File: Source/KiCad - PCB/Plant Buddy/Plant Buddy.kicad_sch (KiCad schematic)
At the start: 25 parts, among them J1 Screw_Terminal_01x02, Q1 AO3401, U1 AMS1117-3.3, U2 TLC555xD

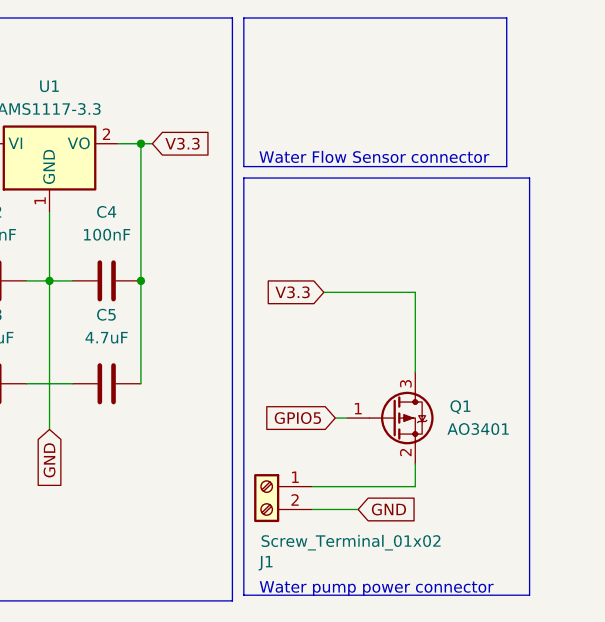
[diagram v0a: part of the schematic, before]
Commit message: Added water flow sensor connector
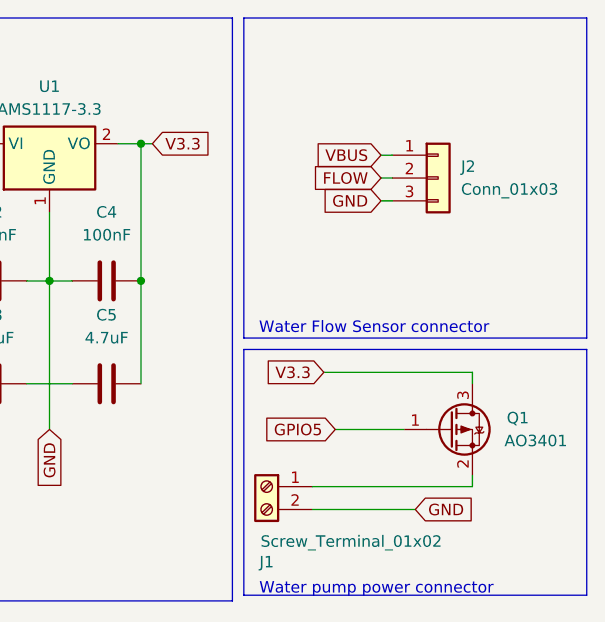
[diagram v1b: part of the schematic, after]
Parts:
- added J2: Conn_01x03, Connector_Hirose:Hirose_DF13-03P-1.25DSA_1x03_P1.25mm_Vertical, symbol Connector_Generic:Conn_01x03
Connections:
- net GND: now also J2.3 (Pin_3)
- net VBUS: now also J2.1 (Pin_1)
- new net FLOW: J2.2 (Pin_2)
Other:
- moved on the sheet: Q1
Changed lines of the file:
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@@
 	(rectangle
 		(start 212.09 13.97)
-		(end 241.3 30.48)
+		(end 250.19 49.53)
 		(stroke
 			(width 0)
@@
 	)
 	(rectangle
-		(start 212.09 31.75)
-		(end 243.84 78.105)
+		(start 212.09 50.8)
+		(end 250.19 78.105)
 		(stroke
 			(width 0)
@@
 	(text "Water Flow Sensor connector"
 		(exclude_from_sim no)
-		(at 226.568 29.718 0)
+		(at 226.568 48.514 0)
 		(effects
 			(font
@@
 	(wire
 		(pts
-			(xy 231.14 66.04) (xy 231.14 63.5)
+			(xy 237.49 66.04) (xy 237.49 64.77)
 		)
 		(stroke
@@
 	(wire
 		(pts
-			(xy 219.71 66.04) (xy 231.14 66.04)
+			(xy 219.71 66.04) (xy 237.49 66.04)
 		)
 		(stroke
@@
 	(wire
 		(pts
+			(xy 227.33 31.75) (xy 228.6 31.75)
+		)
+		(stroke
+			(width 0)
+			(type default)
+		)
+	)
+	(wire
+		(pts
 			(xy 190.5 35.56) (xy 190.5 59.69)
 		)
@@
 	(wire
 		(pts
-			(xy 219.71 68.58) (xy 224.79 68.58)
+			(xy 219.71 68.58) (xy 231.14 68.58)
 		)
 		(stroke
@@
 	(wire
 		(pts
+			(xy 227.33 29.21) (xy 228.6 29.21)
+		)
+		(stroke
+			(width 0)
+			(type default)
+		)
+	)
+	(wire
+		(pts
 			(xy 143.51 44.45) (xy 143.51 43.18)
 		)
@@
 	(wire
 		(pts
-			(xy 231.14 44.45) (xy 231.14 53.34)
+			(xy 237.49 53.34) (xy 237.49 54.61)
 		)
 		(stroke
@@
 	(wire
 		(pts
+			(xy 227.33 34.29) (xy 228.6 34.29)
+		)
+		(stroke
+			(width 0)
+			(type default)
+		)
+	)
+	(wire
+		(pts
 			(xy 118.11 62.23) (xy 127 62.23)
 		)
@@
 	(wire
 		(pts
-			(xy 220.98 44.45) (xy 231.14 44.45)
+			(xy 220.98 53.34) (xy 237.49 53.34)
 		)
 		(stroke
@@
 	(wire
 		(pts
-			(xy 222.25 58.42) (xy 223.52 58.42)
+			(xy 222.25 59.69) (xy 229.87 59.69)
 		)
 		(stroke
@@
 		)
 	)
+	(global_label "FLOW"
+		(shape input)
+		(at 227.33 31.75 180)
+		(fields_autoplaced yes)
+		(effects
+			(font
+				(size 1.27 1.27)
+			)
+			(justify right)
+		)
+		(property "Intersheetrefs" "${INTERSHEET_REFS}"
+			(at 219.4462 31.75 0)
+			(hide yes)
+			(show_name no)
+			(do_not_autoplace no)
+			(effects
+				(font
+					(size 1.27 1.27)
+				)
+				(justify right)
+			)
+		)
+	)
 	(global_label "VBAT"
 		(shape input)
@@
 		)
 	)
+	(global_label "VBUS"
+		(shape input)
+		(at 227.33 29.21 180)
+		(fields_autoplaced yes)
+		(effects
+			(font
+				(size 1.27 1.27)
+			)
+			(justify right)
+		)
+		(property "Intersheetrefs" "${INTERSHEET_REFS}"
+			(at 219.4462 29.21 0)
+			(hide yes)
+			(show_name no)
+			(do_not_autoplace no)
+			(effects
+				(font
+					(size 1.27 1.27)
+				)
+				(justify right)
+			)
+		)
+	)
 	(global_label "V3.3"
 		(shape input)
@@
 	(global_label "V3.3"
 		(shape input)
-		(at 220.98 44.45 180)
+		(at 220.98 53.34 180)
 		(fields_autoplaced yes)
 		(effects
@@
 		)
 		(property "Intersheetrefs" "${INTERSHEET_REFS}"
-			(at 213.8824 44.45 0)
+			(at 213.8824 53.34 0)
 			(hide yes)
 			(show_name no)
@@
 	(global_label "GND"
 		(shape input)
+		(at 227.33 34.29 180)
+		(fields_autoplaced yes)
+		(effects
+			(font
+				(size 1.27 1.27)
+			)
+			(justify right)
+		)
+		(property "Intersheetrefs" "${INTERSHEET_REFS}"
+			(at 220.4743 34.29 0)
+			(hide yes)
+			(show_name no)
+			(do_not_autoplace no)
+			(effects
+				(font
+					(size 1.27 1.27)
+				)
+				(justify right)
+			)
+		)
+	)
+	(global_label "GND"
+		(shape input)
 		(at 39.37 68.58 0)
 		(fields_autoplaced yes)
@@
 	(global_label "GND"
 		(shape input)
-		(at 224.79 68.58 0)
+		(at 231.14 68.58 0)
 		(fields_autoplaced yes)
 		(effects
@@
 		)
 		(property "Intersheetrefs" "${INTERSHEET_REFS}"
-			(at 231.6457 68.58 0)
+			(at 237.9957 68.58 0)
 			(hide yes)
 			(show_name no)
@@
 	(global_label "GPIO5"
 		(shape input)
-		(at 222.25 58.42 180)
+		(at 222.25 59.69 180)
 		(fields_autoplaced yes)
 		(effects
@@
 		)
 		(property "Intersheetrefs" "${INTERSHEET_REFS}"
-			(at 213.58 58.42 0)
+			(at 213.58 59.69 0)
 			(hide yes)
 			(show_name no)
@@
 	)
 	(symbol
+		(lib_id "Connector_Generic:Conn_01x03")
+		(at 233.68 31.75 0)
+		(unit 1)
+		(body_style 1)
+		(exclude_from_sim no)
+		(in_bom yes)
+		(on_board yes)
+		(in_pos_files yes)
+		(dnp no)
+		(fields_autoplaced yes)
+		(property "Reference" "J2"
+			(at 236.22 30.4799 0)
+			(show_name no)
+			(do_not_autoplace no)
+			(effects
+				(font
+					(size 1.27 1.27)
+				)
+				(justify left)
+			)
+		)
+		(property "Value" "Conn_01x03"
+			(at 236.22 33.0199 0)
+			(show_name no)
+			(do_not_autoplace no)
+			(effects
+				(font
+					(size 1.27 1.27)
+				)
+				(justify left)
+			)
+		)
+		(property "Footprint" "Connector_Hirose:Hirose_DF13-03P-1.25DSA_1x03_P1.25mm_Vertical"
+			(at 233.68 31.75 0)
+			(hide yes)
+			(show_name no)
+			(do_not_autoplace no)
+			(effects
+				(font
+					(size 1.27 1.27)
+				)
+			)
+		)
+		(property "Datasheet" ""
+			(at 233.68 31.75 0)
+			(hide yes)
+			(show_name no)
+			(do_not_autoplace no)
+			(effects
+				(font
+					(size 1.27 1.27)
+				)
+			)
+		)
+		(property "Description" "Generic connector, single row, 01x03, script generated (kicad-library-utils/schlib/autogen/connector/)"
+			(at 233.68 31.75 0)
+			(hide yes)
+			(show_name no)
+			(do_not_autoplace no)
+			(effects
+				(font
+					(size 1.27 1.27)
+				)
+			)
+		)
+		(pin "2"
+		)
+		(pin "1"
+		)
+		(pin "3"
+		)
+		(instances
+			(project "Plant Buddy"
+				(path "/4f94c837-6daf-4f59-97d2-d69d62a434e7"
+					(reference "J2")
+					(unit 1)
+				)
+			)
+		)
+	)
+	(symbol
 		(lib_id "Library:S2B-PH-SM4-TB")
 		(at 31.75 25.4 180)
@@
 	(symbol
 		(lib_id "Transistor_FET:VP0610T")
-		(at 228.6 58.42 0)
+		(at 234.95 59.69 0)
 		(unit 1)
 		(body_style 1)
@@
 		(dnp no)
 		(property "Reference" "Q1"
-			(at 234.95 57.15 0)
+			(at 241.3 58.42 0)
 			(show_name no)
 			(do_not_autoplace no)
@@
 		)
 		(property "Value" "AO3401"
-			(at 234.696 59.69 0)
+			(at 241.046 60.96 0)
 			(show_name no)
 			(do_not_autoplace no)
@@
 		)
 		(property "Footprint" "Package_TO_SOT_SMD:SOT-23"
-			(at 233.68 60.325 0)
+			(at 240.03 61.595 0)
 			(hide yes)
 			(show_name no)
@@
 		)
 		(property "Datasheet" "http://www.vishay.com/docs/70209/70209.pdf"
-			(at 233.68 62.23 0)
+			(at 240.03 63.5 0)
 			(hide yes)
 			(show_name no)
@@
 		)
 		(property "Description" "-0.18A Id, -60V Vds, P-Channel MOSFET, SOT-23"
-			(at 228.6 58.42 0)
+			(at 234.95 59.69 0)
 			(hide yes)
 			(show_name no)

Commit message: Finished Schematic and PCB
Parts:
- added C10: 4.7uF, Capacitor_SMD:C_1206_3216Metric_Pad1.33x1.80mm_HandSolder, symbol Device:C
- added C11, C12: 100nF, Capacitor_SMD:C_1206_3216Metric_Pad1.33x1.80mm_HandSolder, symbol Device:C
- added J3: Conn_02x04_Counter_Clockwise, Connector_PinSocket_2.54mm:PinSocket_2x04_P2.54mm_Vertical, symbol Connector_Generic:Conn_02x04_Counter_Clockwise
- added R7: 2K, Resistor_SMD:R_0805_2012Metric_Pad1.20x1.40mm_HandSolder, symbol Device:R
- added R8: 3K, Resistor_SMD:R_0805_2012Metric_Pad1.20x1.40mm_HandSolder, symbol Device:R
- added R9: 10K, Resistor_SMD:R_0805_2012Metric_Pad1.20x1.40mm_HandSolder, symbol Device:R
- added SW2: (EN), Button_Switch_THT:SW_PUSH_6mm_H13mm, symbol Switch:SW_Push
- added U4: (no value), Library:ESP32 DevKit, symbol Library:ESP32_DevKit
- C2, C4, C6, C7, C8, C9: footprint (none) -> Capacitor_SMD:C_0805_2012Metric_Pad1.18x1.45mm_HandSolder
- C3, C5: footprint (none) -> Capacitor_SMD:C_1206_3216Metric_Pad1.33x1.80mm_HandSolder
- D1: footprint (none) -> Diode_SMD:D_SOD-323_HandSoldering
- J2: footprint Connector_Hirose:Hirose_DF13-03P-1.25DSA_1x03_P1.25mm_Vertical -> Connector_PinSocket_2.54mm:PinSocket_1x03_P2.54mm_Vertical
- R1, R2, R3, R4, R5: footprint (none) -> Resistor_SMD:R_0805_2012Metric_Pad1.20x1.40mm_HandSolder
- R6: footprint (none) -> Resistor_THT:R_Axial_DIN0207_L6.3mm_D2.5mm_P7.62mm_Horizontal
- U2: footprint Package_SO:SOIC-8_3.9x4.9mm_P1.27mm -> Package_SO:SOP-8_3.76x4.96mm_P1.27mm
- renumbered BUCK_IN to BUCK_IN1, BUCK_OUT to BUCK_OUT1
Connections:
- net FLOW: now also R7.2, R8.1, U4.13 (IO13); no longer J2.2 (Pin_2)
- net GND: now also C1.2, C3.2, C4.2, C5.1, C9.1, R3.2, C10.1, C11.1, C12.2, J3.1 (Pin_1), R8.2, SW2.1, U4.14 (GND), U4.29 (GND); no longer C1.1, C4.1, C9.2, R3.1
- net GPIO32: now also R3.1, U4.6 (IO32); no longer R3.2
- net GPIO33: now also U4.7 (IO33)
- net GPIO5: now also U4.23 (IO5)
- net V3.3: now also C4.1, R9.1; no longer C4.2
- net VBAT: now also C1.1; no longer C1.2
- net VBUS: now also J3.8 (Pin_8)
- net at R6.2, U2.2 (TRIG), U2.6 (THRES): now also C9.2; no longer C9.1
- new net: C10.2, C11.2, U4.30 (3.3V)
- new net: J2.2 (Pin_2), R7.1
- new net: C12.1, R9.2, SW2.2, U4.1 (EN)
- new net GPIO1: J3.7 (Pin_7), U4.18 (IO1)
- new net GPIO3: J3.2 (Pin_2), U4.19 (IO3)
- no-connect marks 0 -> 4
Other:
- note added: "ESP32"
- note added: "SIM800L"
- moved on the sheet: C1, C4, C9, J2, R3

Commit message: Edited PCB and schematics.
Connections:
- net GND: now also J2.1 (Pin_1); no longer J2.3 (Pin_3)
- net VBUS: now also J2.3 (Pin_3); no longer J2.1 (Pin_1)
- net GPIO25: now reaches U4.8 (IO25)
- net GPIO25: now also J3.4 (Pin_4)
- no-connect marks 4 -> 3

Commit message: Finished the firmware and modified the schematics and the PCB
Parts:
- added R10: 220, Resistor_SMD:R_0805_2012Metric_Pad1.20x1.40mm_HandSolder, symbol Device:R
- added U3: PC817, Package_DIP:DIP-4_W7.62mm, symbol Isolator:PC817
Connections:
- net GND: now also U3.2
- net GPIO5: now also R10.1; no longer Q1.1 (G)
- net V3.3: no longer Q1.3 (D)
- net VBUS: now also Q1.2 (S), U3.4
- net at J1.1 (Pin_1): now also Q1.3 (D); no longer Q1.2 (S)
- new net: R10.2, U3.1
- new net: Q1.1 (G), U3.3
- no-connect marks 3 -> 22
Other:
- moved on the sheet: J1, Q1

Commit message: Designed 3D case
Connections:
- net VBUS: now also J2.2 (Pin_2); no longer J2.3 (Pin_3)
- net at R7.1: now also J2.3 (Pin_3); no longer J2.2 (Pin_2)
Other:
- moved on the sheet: J2, R7, R8
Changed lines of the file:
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@@
 	)
 	(junction
-		(at 226.06 35.56)
+		(at 217.17 34.29)
 		(diameter 0)
 		(color 0 0 0 0)
@@
 	(wire
 		(pts
-			(xy 226.06 24.13) (xy 226.06 26.67)
+			(xy 217.17 21.59) (xy 217.17 25.4)
 		)
 		(stroke
@@
 	(wire
 		(pts
-			(xy 226.06 34.29) (xy 226.06 35.56)
+			(xy 217.17 33.02) (xy 217.17 34.29)
 		)
 		(stroke
@@
 	(wire
 		(pts
-			(xy 226.06 45.72) (xy 233.68 45.72)
+			(xy 217.17 44.45) (xy 224.79 44.45)
 		)
 		(stroke
@@
 	(wire
 		(pts
-			(xy 226.06 35.56) (xy 226.06 36.83)
+			(xy 217.17 34.29) (xy 217.17 35.56)
 		)
 		(stroke
@@
 	(wire
 		(pts
-			(xy 74.93 31.75) (xy 74.93 35.56)
+			(xy 217.17 21.59) (xy 238.76 21.59)
 		)
 		(stroke
@@
 	(wire
 		(pts
-			(xy 226.06 35.56) (xy 233.68 35.56)
+			(xy 74.93 31.75) (xy 74.93 35.56)
 		)
 		(stroke
@@
 	(wire
 		(pts
-			(xy 125.73 43.18) (xy 128.27 43.18)
+			(xy 217.17 34.29) (xy 224.79 34.29)
 		)
 		(stroke
@@
 	(wire
 		(pts
-			(xy 220.98 64.77) (xy 231.14 64.77)
+			(xy 125.73 43.18) (xy 128.27 43.18)
 		)
 		(stroke
@@
 	(wire
 		(pts
-			(xy 238.76 24.13) (xy 226.06 24.13)
+			(xy 220.98 64.77) (xy 231.14 64.77)
 		)
 		(stroke
@@
 	(wire
 		(pts
+			(xy 237.49 19.05) (xy 238.76 19.05)
+		)
+		(stroke
+			(width 0)
+			(type default)
+		)
+	)
+	(wire
+		(pts
 			(xy 271.78 27.94) (xy 274.32 27.94)
 		)
@@
 	(wire
 		(pts
-			(xy 226.06 44.45) (xy 226.06 45.72)
+			(xy 217.17 43.18) (xy 217.17 44.45)
 		)
 		(stroke
@@
 	(wire
 		(pts
-			(xy 237.49 26.67) (xy 238.76 26.67)
-		)
-		(stroke
-			(width 0)
-			(type default)
-		)
-	)
-	(wire
-		(pts
 			(xy 74.93 147.32) (xy 78.74 147.32)
 		)
@@
 	(wire
 		(pts
-			(xy 237.49 21.59) (xy 238.76 21.59)
+			(xy 237.49 16.51) (xy 238.76 16.51)
 		)
 		(stroke
@@
 	(global_label "FLOW"
 		(shape input)
-		(at 233.68 35.56 0)
+		(at 224.79 34.29 0)
 		(fields_autoplaced yes)
 		(effects
@@
 		)
 		(property "Intersheetrefs" "${INTERSHEET_REFS}"
-			(at 241.5638 35.56 0)
+			(at 232.6738 34.29 0)
 			(hide yes)
 			(show_name no)
@@
 	(global_label "GND"
 		(shape input)
-		(at 233.68 45.72 0)
+		(at 224.79 44.45 0)
 		(fields_autoplaced yes)
 		(effects
@@
 		)
 		(property "Intersheetrefs" "${INTERSHEET_REFS}"
-			(at 240.5357 45.72 0)
+			(at 231.6457 44.45 0)
 			(hide yes)
 			(show_name no)
@@
 	(global_label "GND"
 		(shape input)
-		(at 237.49 21.59 180)
+		(at 237.49 16.51 180)
 		(fields_autoplaced yes)
 		(effects
@@
 		)
 		(property "Intersheetrefs" "${INTERSHEET_REFS}"
-			(at 230.6343 21.59 0)
+			(at 230.6343 16.51 0)
 			(hide yes)
 			(show_name no)
@@
 	(global_label "VBUS"
 		(shape input)
-		(at 237.49 26.67 180)
+		(at 237.49 19.05 180)
 		(fields_autoplaced yes)
 		(effects
@@
 		)
 		(property "Intersheetrefs" "${INTERSHEET_REFS}"
-			(at 229.6062 26.67 0)
+			(at 229.6062 19.05 0)
 			(hide yes)
 			(show_name no)
@@
 	(symbol
 		(lib_id "Connector_Generic:Conn_01x03")
-		(at 243.84 24.13 0)
+		(at 243.84 19.05 0)
 		(unit 1)
 		(body_style 1)
@@
 		(dnp no)
 		(property "Reference" "J2"
-			(at 233.934 15.748 0)
+			(at 234.188 27.432 0)
 			(show_name no)
 			(do_not_autoplace no)
@@
 		)
 		(property "Value" "Conn_01x03"
-			(at 233.934 18.288 0)
+			(at 234.188 29.972 0)
 			(show_name no)
 			(do_not_autoplace no)
@@
 		)
 		(property "Footprint" "Connector_PinSocket_2.54mm:PinSocket_1x03_P2.54mm_Vertical"
-			(at 243.84 24.13 0)
+			(at 243.84 19.05 0)
 			(hide yes)
 			(show_name no)
@@
 		)
 		(property "Datasheet" ""
-			(at 243.84 24.13 0)
+			(at 243.84 19.05 0)
 			(hide yes)
 			(show_name no)
@@
 		)
 		(property "Description" "Generic connector, single row, 01x03, script generated (kicad-library-utils/schlib/autogen/connector/)"
-			(at 243.84 24.13 0)
+			(at 243.84 19.05 0)
 			(hide yes)
 			(show_name no)
@@
 	(symbol
 		(lib_id "Device:R")
-		(at 226.06 30.48 0)
+		(at 217.17 29.21 0)
 		(unit 1)
 		(body_style 1)
@@
 		(fields_autoplaced yes)
 		(property "Reference" "R7"
-			(at 228.6 29.2099 0)
+			(at 219.71 27.9399 0)
 			(show_name no)
 			(do_not_autoplace no)
@@
 		)
 		(property "Value" "2K"
-			(at 228.6 31.7499 0)
+			(at 219.71 30.4799 0)
 			(show_name no)
 			(do_not_autoplace no)
@@
 		)
 		(property "Footprint" "Resistor_SMD:R_0805_2012Metric_Pad1.20x1.40mm_HandSolder"
-			(at 224.282 30.48 90)
+			(at 215.392 29.21 90)
 			(hide yes)
 			(show_name no)
@@
 		)
 		(property "Datasheet" ""
-			(at 226.06 30.48 0)
+			(at 217.17 29.21 0)
 			(hide yes)
 			(show_name no)
@@
 		)
 		(property "Description" "Resistor"
-			(at 226.06 30.48 0)
+			(at 217.17 29.21 0)
 			(hide yes)
 			(show_name no)
@@
 	(symbol
 		(lib_id "Device:R")
-		(at 226.06 40.64 0)
+		(at 217.17 39.37 0)
 		(unit 1)
 		(body_style 1)
@@
 		(fields_autoplaced yes)
 		(property "Reference" "R8"
-			(at 228.6 39.3699 0)
+			(at 219.71 38.0999 0)
 			(show_name no)
 			(do_not_autoplace no)
@@
 		)
 		(property "Value" "3K"
-			(at 228.6 41.9099 0)
+			(at 219.71 40.6399 0)
 			(show_name no)
 			(do_not_autoplace no)
@@
 		)
 		(property "Footprint" "Resistor_SMD:R_0805_2012Metric_Pad1.20x1.40mm_HandSolder"
-			(at 224.282 40.64 90)
+			(at 215.392 39.37 90)
 			(hide yes)
 			(show_name no)
@@
 		)
 		(property "Datasheet" ""
-			(at 226.06 40.64 0)
+			(at 217.17 39.37 0)
 			(hide yes)
 			(show_name no)
@@
 		)
 		(property "Description" "Resistor"
-			(at 226.06 40.64 0)
+			(at 217.17 39.37 0)
 			(hide yes)
 			(show_name no)

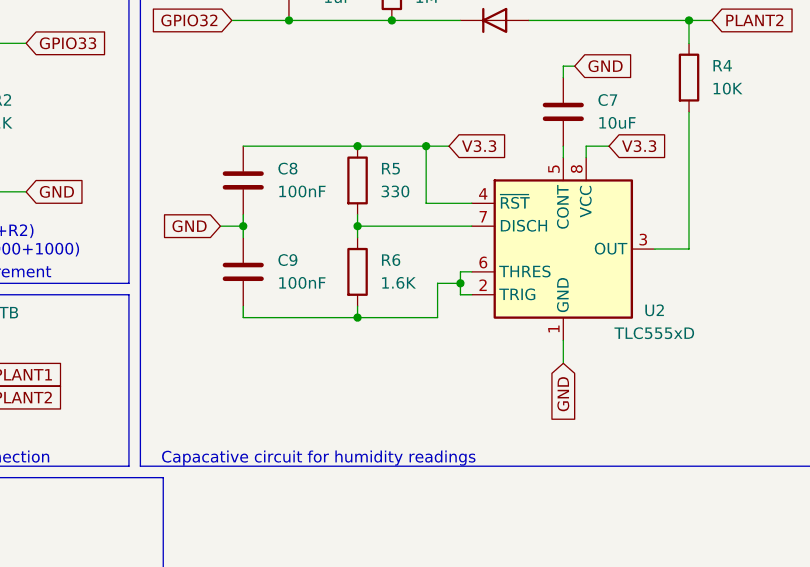
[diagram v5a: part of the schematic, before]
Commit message: Added BOM
Added the BOM, and modified the schematics to have a resistor that I can buy.
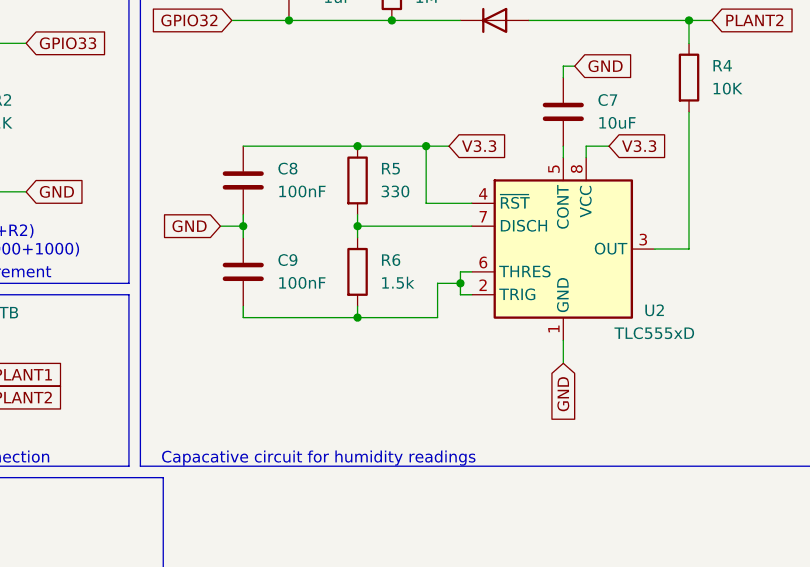
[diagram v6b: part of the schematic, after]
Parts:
- R6: value 1.6K -> 1.5k
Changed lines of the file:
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@@
 			)
 		)
-		(property "Value" "1.6K"
+		(property "Value" "1.5k"
 			(at 120.65 58.4199 0)
 			(show_name no)
